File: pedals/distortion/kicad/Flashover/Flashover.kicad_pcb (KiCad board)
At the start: 4 copper layers, 87.6 x 84 mm, 95 parts, among them J1 Input, J2 Output, J3 9V DC, J4 SWD, J5 MIDI In, J6 MIDI Out, J7 To control board, K1 G6K-2F-Y 5VDC, K2 G6K-2F-Y 5VDC, Q1 MMBT3904, Q2 MMBT3904, SW5 Footswitch, U1 LM741, U11 H11L1, U2 TL072, U3 L7805, U4 RP2040, U5 W25Q16JVSS, U6 AP2112K-3.3, U7 MCP45HV51-104, U8 MCP45HV51-103, U9 MCP45HV51-103, Y1 12MHz

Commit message: Route five more Flashover main board connections (9 -> 4 open)
+3V3 at U4's top and at the regulator, SDA to U8, HARD_SEL and QSPI SD2.
Removes a dead-end QSPI_SCLK via and stub left by the autorouter.

Co-Authored-By: Claude Opus 5.5 <noreply@anthropic.com>
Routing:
- net +3V3: track 251.1 -> 276.0 mm, vias 22 -> 27
- net Net-(U4-QSPI_SD2): track 0.00 -> 22.6 mm, vias 0 -> 4
- net SDA: track 92.9 -> 111.6 mm, vias 5 -> 7
- net HARD_SEL: track 1.77 -> 16.5 mm, vias 1 -> 2
- net Net-(U4-QSPI_SCLK): track 27.5 -> 26.9 mm, vias 5 -> 4

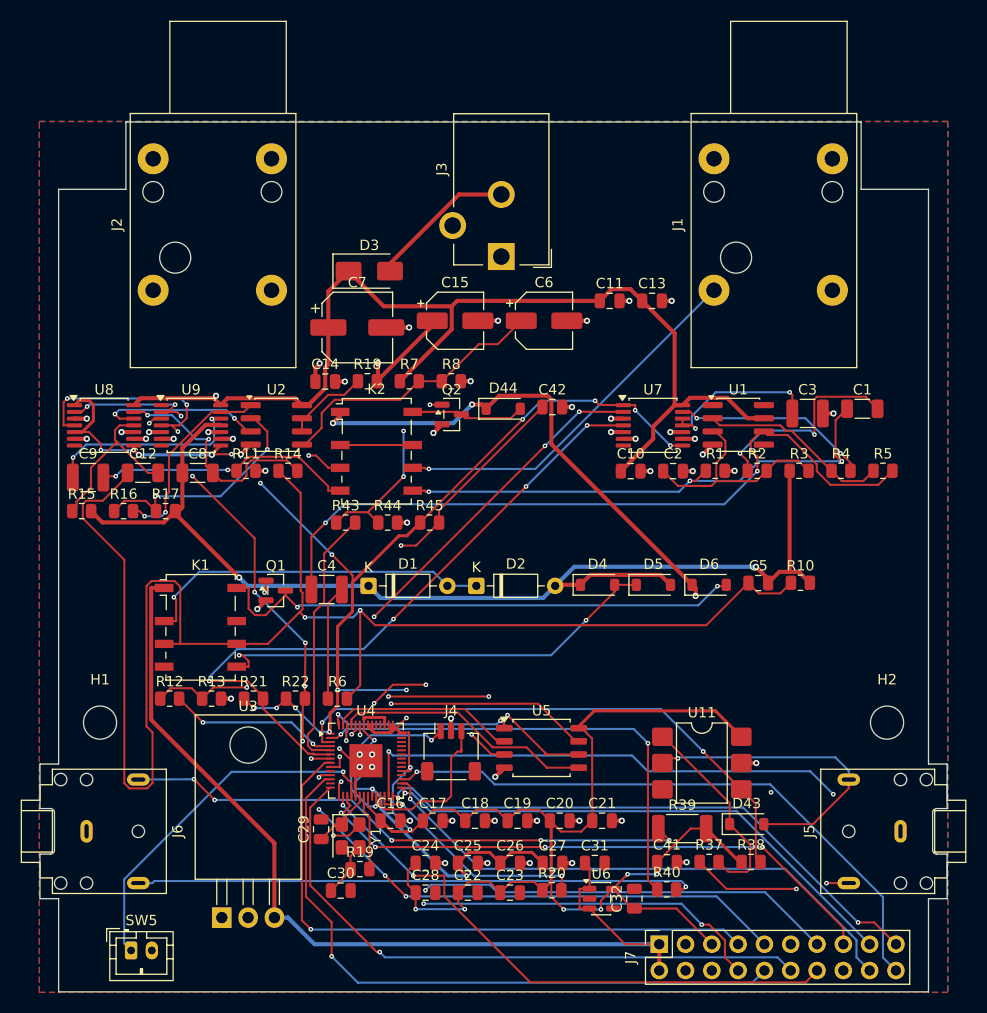
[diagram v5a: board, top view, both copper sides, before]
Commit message: Finish routing the Flashover main board (0 open, 0 errors)
Reroute GAIN/TONE on U4's crowded left side so pins 10 and 13 can escape,
reach U9 pin 1 through a via (moving one SCL segment), and add a ground
stitching via for a cut-off patch of fill. Both boards are now fully routed
and match their schematics.

Co-Authored-By: Claude Opus 5.5 <noreply@anthropic.com>
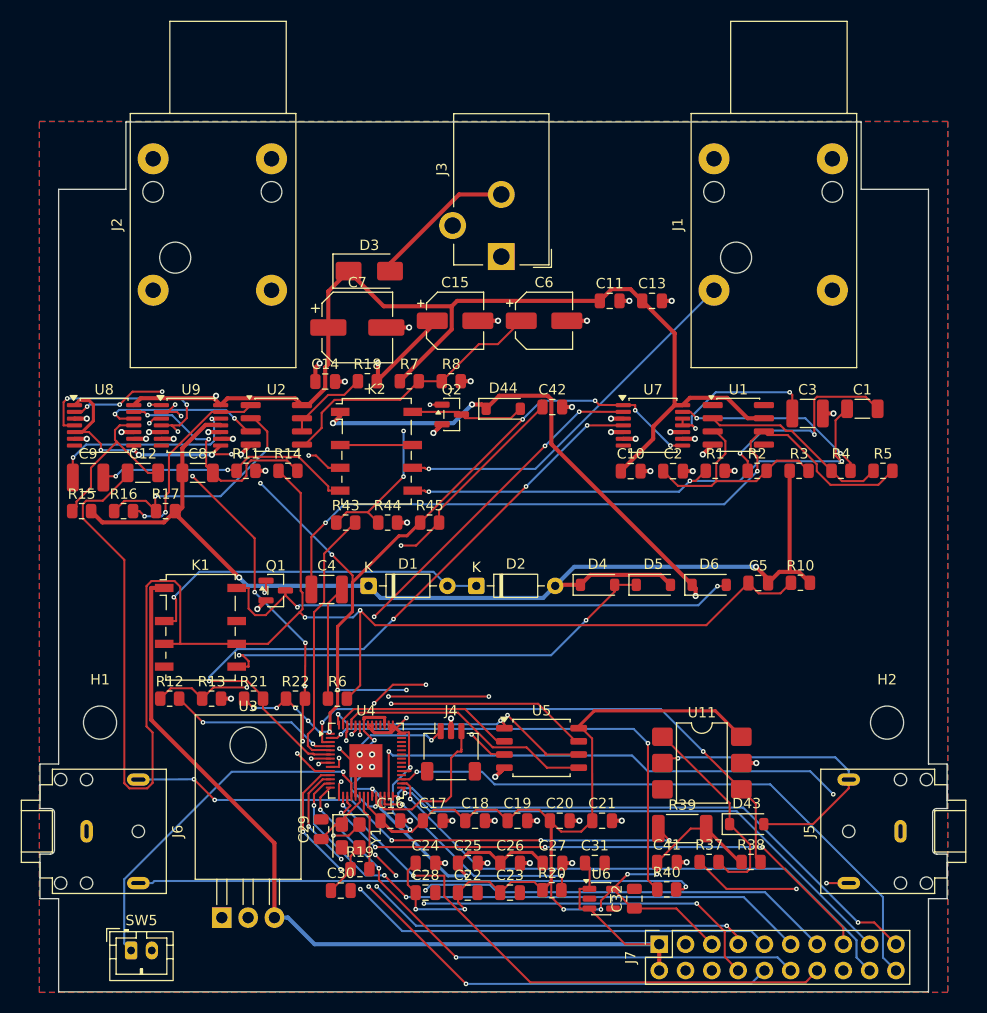
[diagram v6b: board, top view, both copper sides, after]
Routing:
- net TONE_B: track 15.5 -> 55.7 mm, vias 1 -> 3
- net +3V3: track 276.0 -> 286.8 mm, vias 27 -> 30
- net TONE_A: track 62.7 -> 56.7 mm, vias 1 -> 4
- net GAIN_A: track 59.7 -> 53.7 mm, vias 1 -> 3
- net TONE_SW: track 60.1 -> 55.1 mm, vias 1 -> 3
- net GAIN_SW: track 52.7 -> 56.1 mm, vias 4 -> 3
- net SCL: track 98.1 -> 99.2 mm, vias 12 -> 14
- net GAIN_B: track 53.8 -> 53.9 mm, vias 3 -> 5
- net GND: vias 52 -> 53

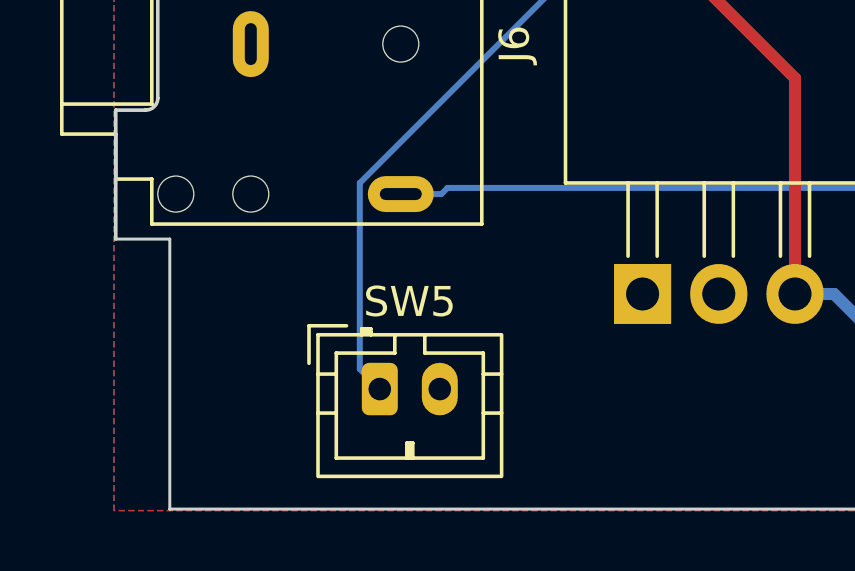
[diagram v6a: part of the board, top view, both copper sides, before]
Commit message: Use a side-entry footswitch connector on the Flashover main board
The upright JST PH header (SW5) sat under the control board with only
5 mm above it for the wires. The side-entry S2B-PH-K-S takes the plug
from the front edge, so it can be connected after stacking. It moves
2.75 mm toward the edge, and the FOOTSW track is shortened to match.
Still 0 unconnected, 0 errors, schematic parity clean.

Co-Authored-By: Claude Opus 5.5 <noreply@anthropic.com>
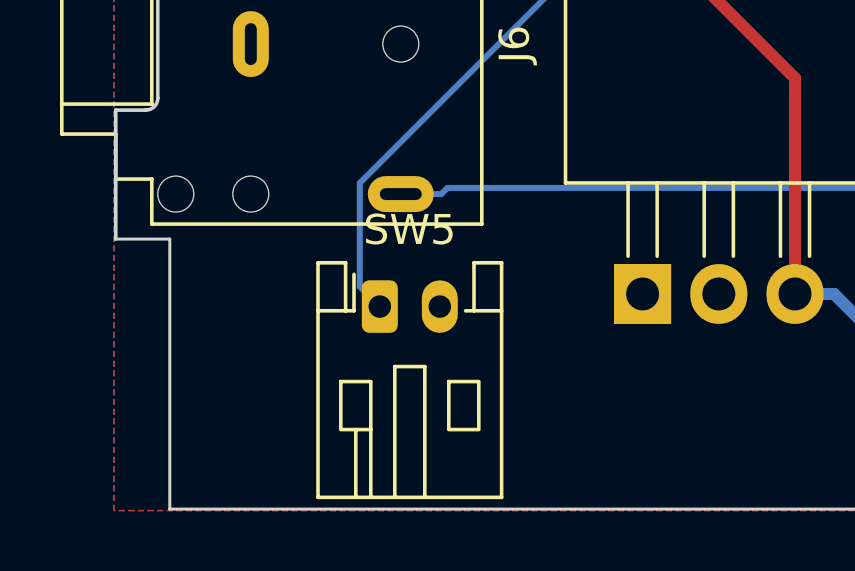
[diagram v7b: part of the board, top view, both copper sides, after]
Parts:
- SW5: footprint Connector_JST:JST_PH_B2B-PH-K_1x02_P2.00mm_Vertical -> Connector_JST:JST_PH_S2B-PH-K_1x02_P2.00mm_Horizontal
- moved SW5 2.75 mm to (112.0, 131.2)
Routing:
- net FOOTSW: track 79.3 -> 76.6 mm
